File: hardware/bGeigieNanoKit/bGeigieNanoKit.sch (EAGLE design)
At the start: 5 parts

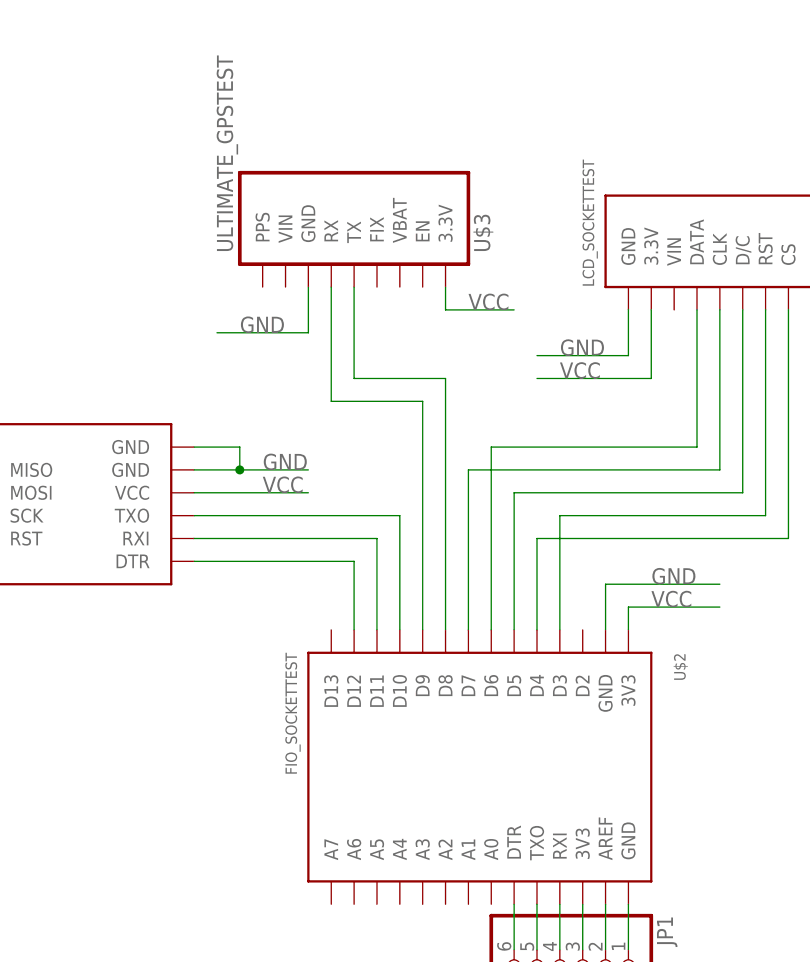
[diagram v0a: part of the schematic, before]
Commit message: library updated with full module footprints. test components removed. board updated to use new library components.
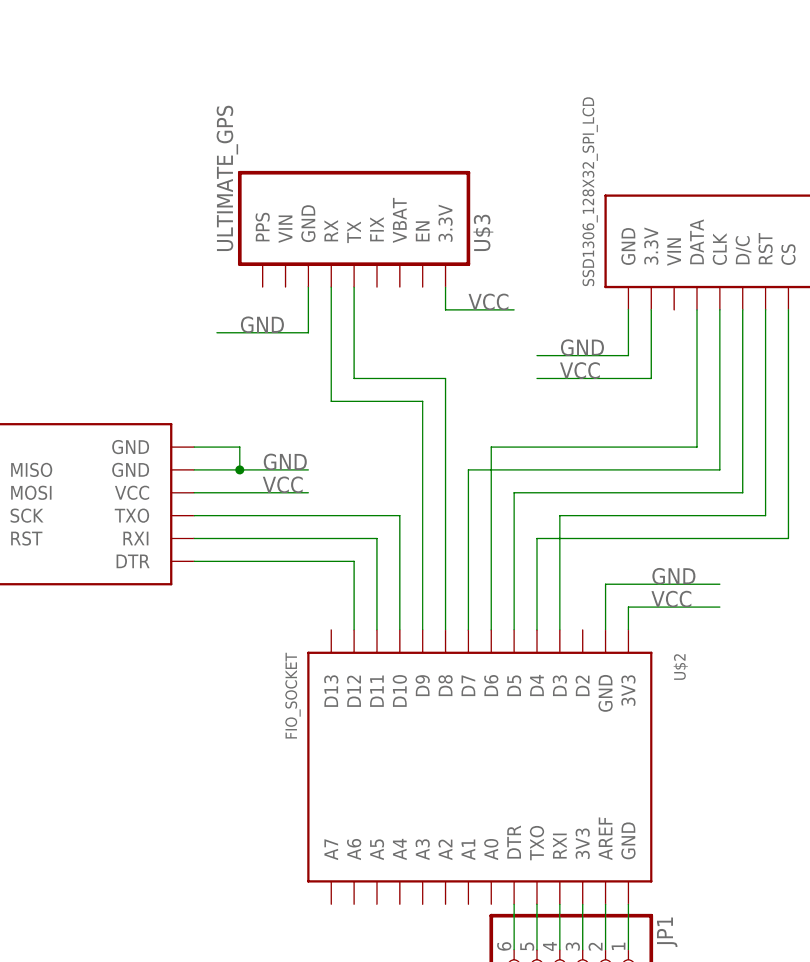
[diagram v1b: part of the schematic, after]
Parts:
- U$1: value OPENLOGTEST -> OPENLOG; device open_hw_sockets:OPENLOGTEST -> open_hw_sockets:OPENLOG
- U$2: value FIO_SOCKETTEST -> FIO_SOCKET; device open_hw_sockets:FIO_SOCKETTEST -> open_hw_sockets:FIO_SOCKET
- U$3: value ULTIMATE_GPSTEST -> ULTIMATE_GPS; device open_hw_sockets:ULTIMATE_GPSTEST -> open_hw_sockets:ULTIMATE_GPS
- U$4: value LCD_SOCKETTEST -> SSD1306_128X32_SPI_LCD; device open_hw_sockets:LCD_SOCKETTEST -> open_hw_sockets:SSD1306_128X32_SPI_LCD
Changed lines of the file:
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@@
 <parts>
 <part name="FRAME1" library="frames" deviceset="FRAME_A_L" device=""/>
-<part name="U$1" library="open_hw_sockets" deviceset="OPENLOG" device="TEST" value="OPENLOGTEST"/>
-<part name="U$4" library="open_hw_sockets" deviceset="LCD_SOCKET" device="TEST" value="LCD_SOCKETTEST"/>
-<part name="U$3" library="open_hw_sockets" deviceset="ULTIMATE_GPS" device="TEST" value="ULTIMATE_GPSTEST"/>
-<part name="U$2" library="open_hw_sockets" deviceset="FIO_SOCKET" device="TEST" value="FIO_SOCKETTEST"/>
+<part name="U$1" library="open_hw_sockets" deviceset="OPENLOG" device="" value="OPENLOG"/>
+<part name="U$4" library="open_hw_sockets" deviceset="SSD1306_128X32_SPI_LCD" device="" value="SSD1306_128X32_SPI_LCD"/>
+<part name="U$3" library="open_hw_sockets" deviceset="ULTIMATE_GPS" device="" value="ULTIMATE_GPS"/>
+<part name="U$2" library="open_hw_sockets" deviceset="FIO_SOCKET" device="" value="FIO_SOCKET"/>
 <part name="JP1" library="pinhead" deviceset="PINHD-1X6" device=""/>
 </parts>

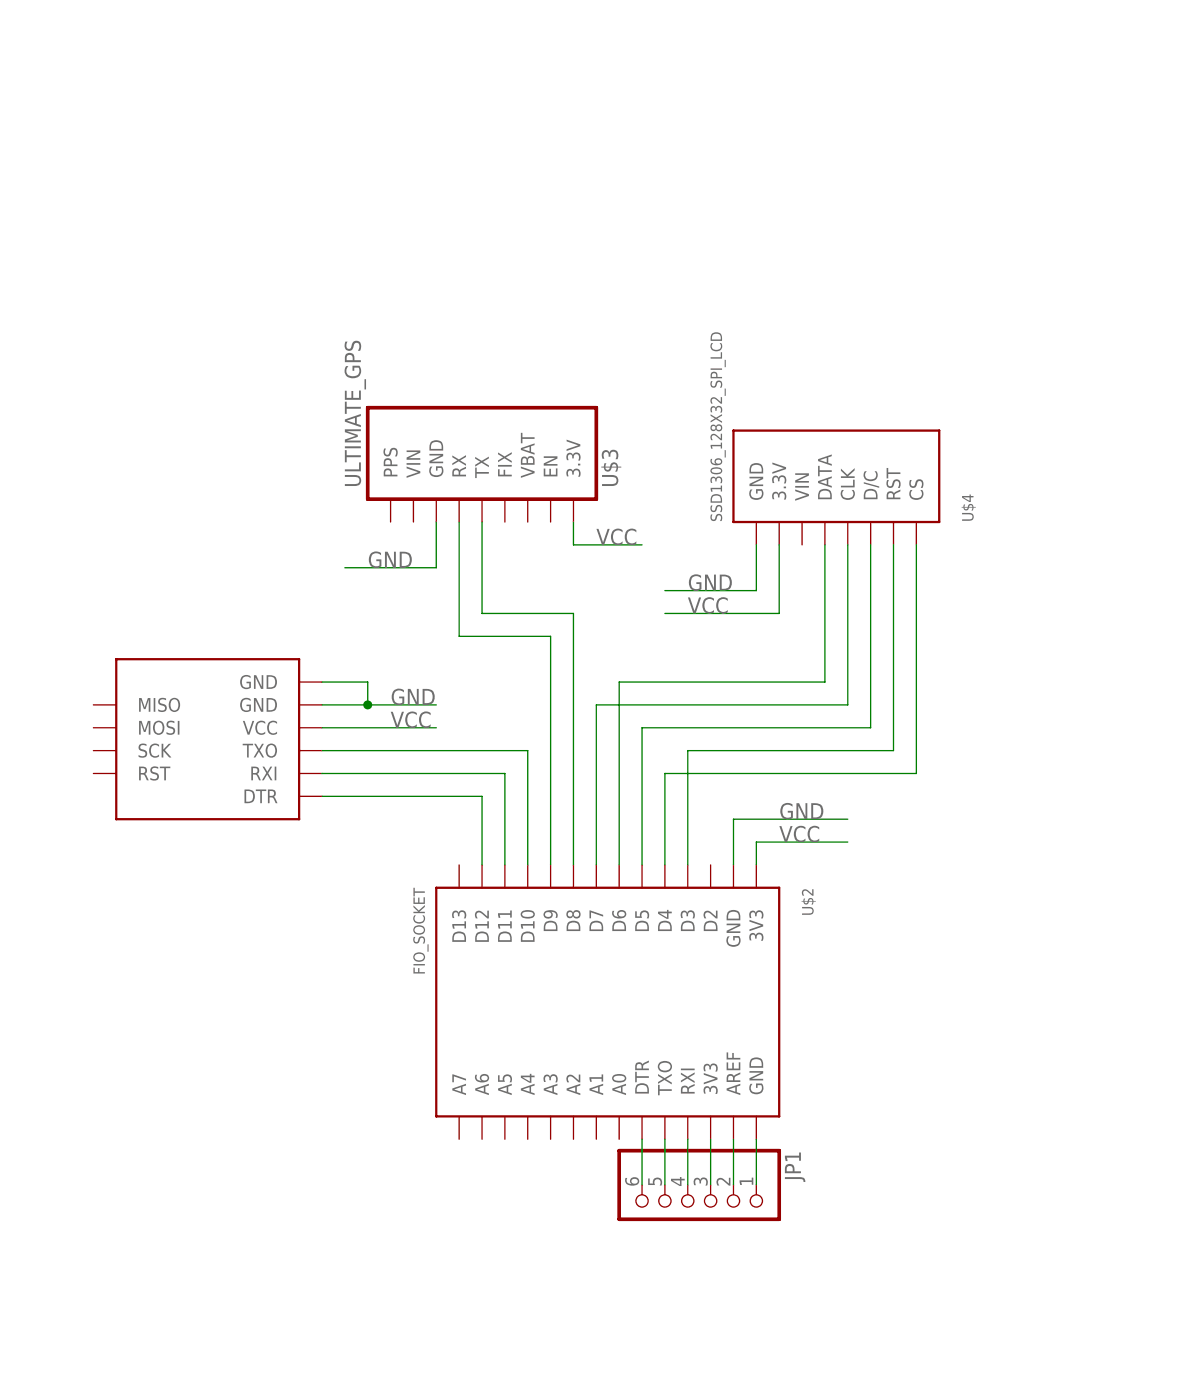
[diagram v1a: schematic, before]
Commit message: updated library footprints with single/double sided options. preliminary component placement on board to verify fit.
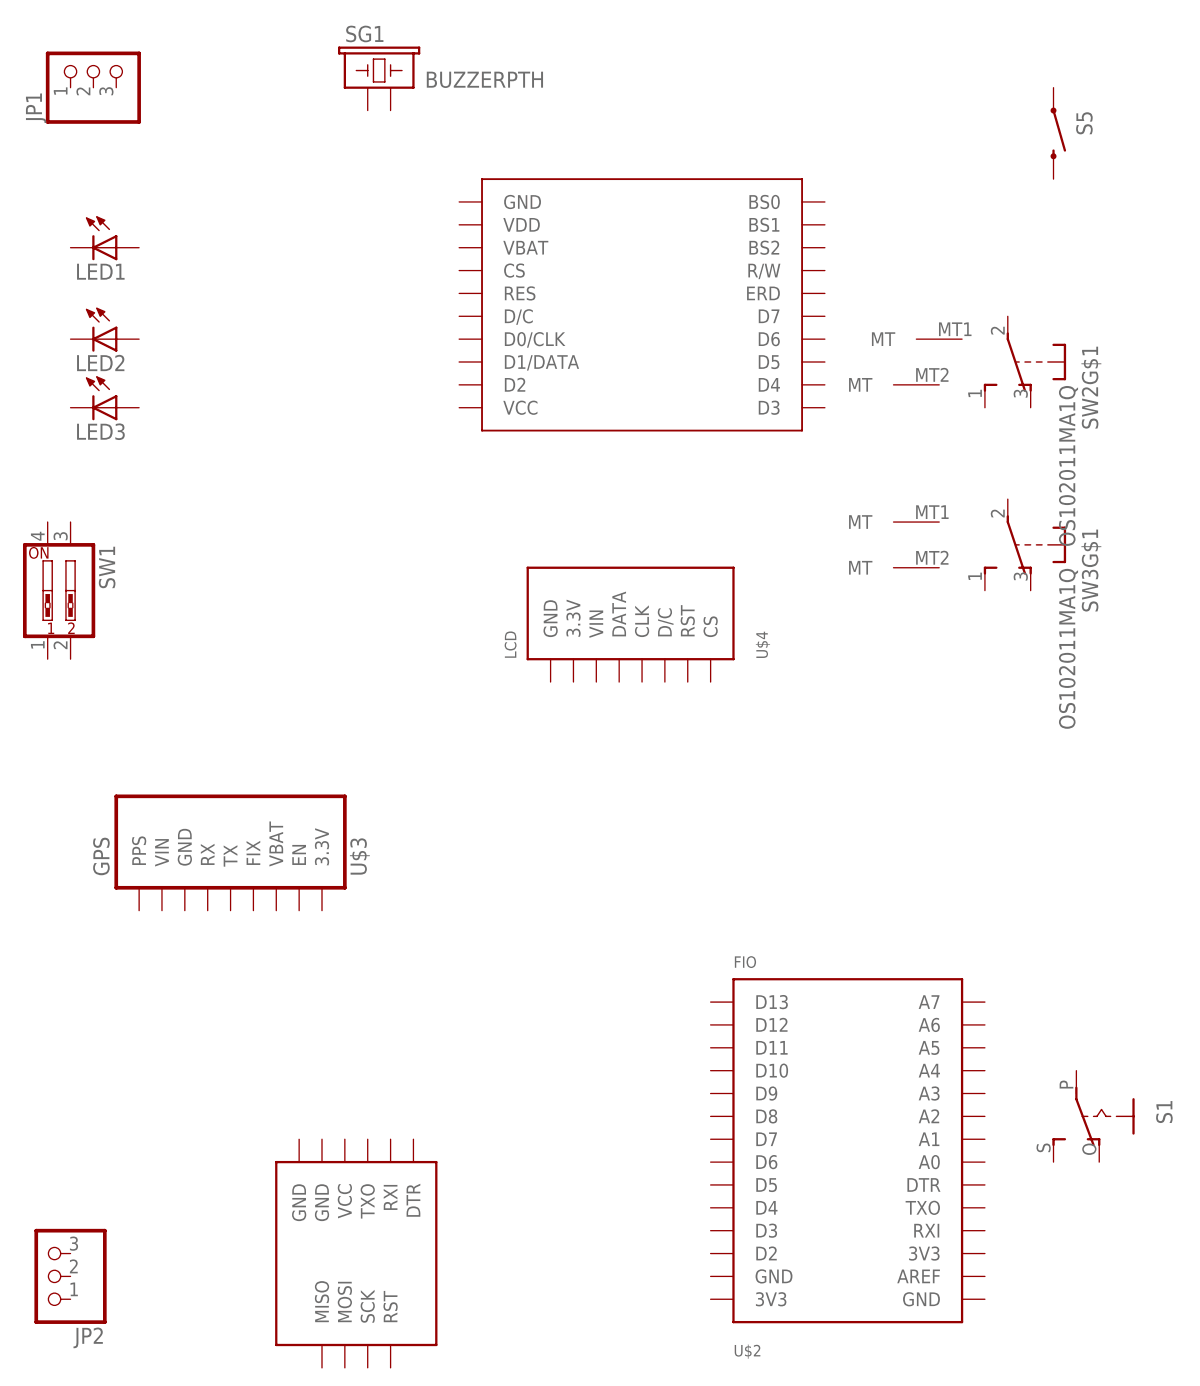
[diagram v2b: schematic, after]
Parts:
- added JP2: (no value), microbuilder:HEADER-1X376MIL
- added LED1, LED2, LED3: (no value), adafruit:LED3MM
- added S1: (no value), adafruit:EG1218S
- added S5: SWITCH-MOMENTARY-2PTH, SparkFun:SWITCH-MOMENTARY-2PTH
- added SG1: BUZZERPTH, SparkFun:BUZZERPTH
- added SW1: (no value), SparkFun:SW_DIP-2
- added SW2, SW3: OS102011MA1Q, adafruit:OS102011MA1Q
- added U$5: SSD1306_128X64_LCDTOP, open_hw_sockets:SSD1306_128X64_LCDTOP
- JP1: device pinhead:PINHD-1X6 -> microbuilder:HEADER-1X376MIL
- U$2: value FIO_SOCKET -> FIO
- U$3: value ULTIMATE_GPS -> GPS
- U$4: value SSD1306_128X32_SPI_LCD -> LCD
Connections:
- removed net GND: U$1.GND@1, U$1.GND@2, U$2.GND@1, U$3.GND, U$4.GND
- removed net N$1: U$1.DTR, U$2.D12
- removed net N$10: U$2.D4, U$4.CS
- removed net N$11: JP1.1, U$2.GND@2
- removed net N$12: JP1.2, U$2.AREF
- removed net N$13: JP1.3, U$2.3V3@2
- removed net N$14: JP1.4, U$2.RXI
- removed net N$15: JP1.5, U$2.TXO
- removed net N$16: JP1.6, U$2.DTR
- removed net N$2: U$1.RXI, U$2.D11
- removed net N$3: U$1.TXO, U$2.D10
- removed net N$4: U$2.D9, U$3.RX
- removed net N$5: U$2.D8, U$3.TX
- removed net N$6: U$2.D6, U$4.DATA
- removed net N$7: U$2.D7, U$4.CLK
- removed net N$8: U$2.D5, U$4.D/C
- removed net N$9: U$2.D3, U$4.RST
- removed net VCC: U$1.VCC, U$2.3V3@1, U$3.3.3V, U$4.3.3V
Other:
- moved on the sheet: U$2, U$3, U$4

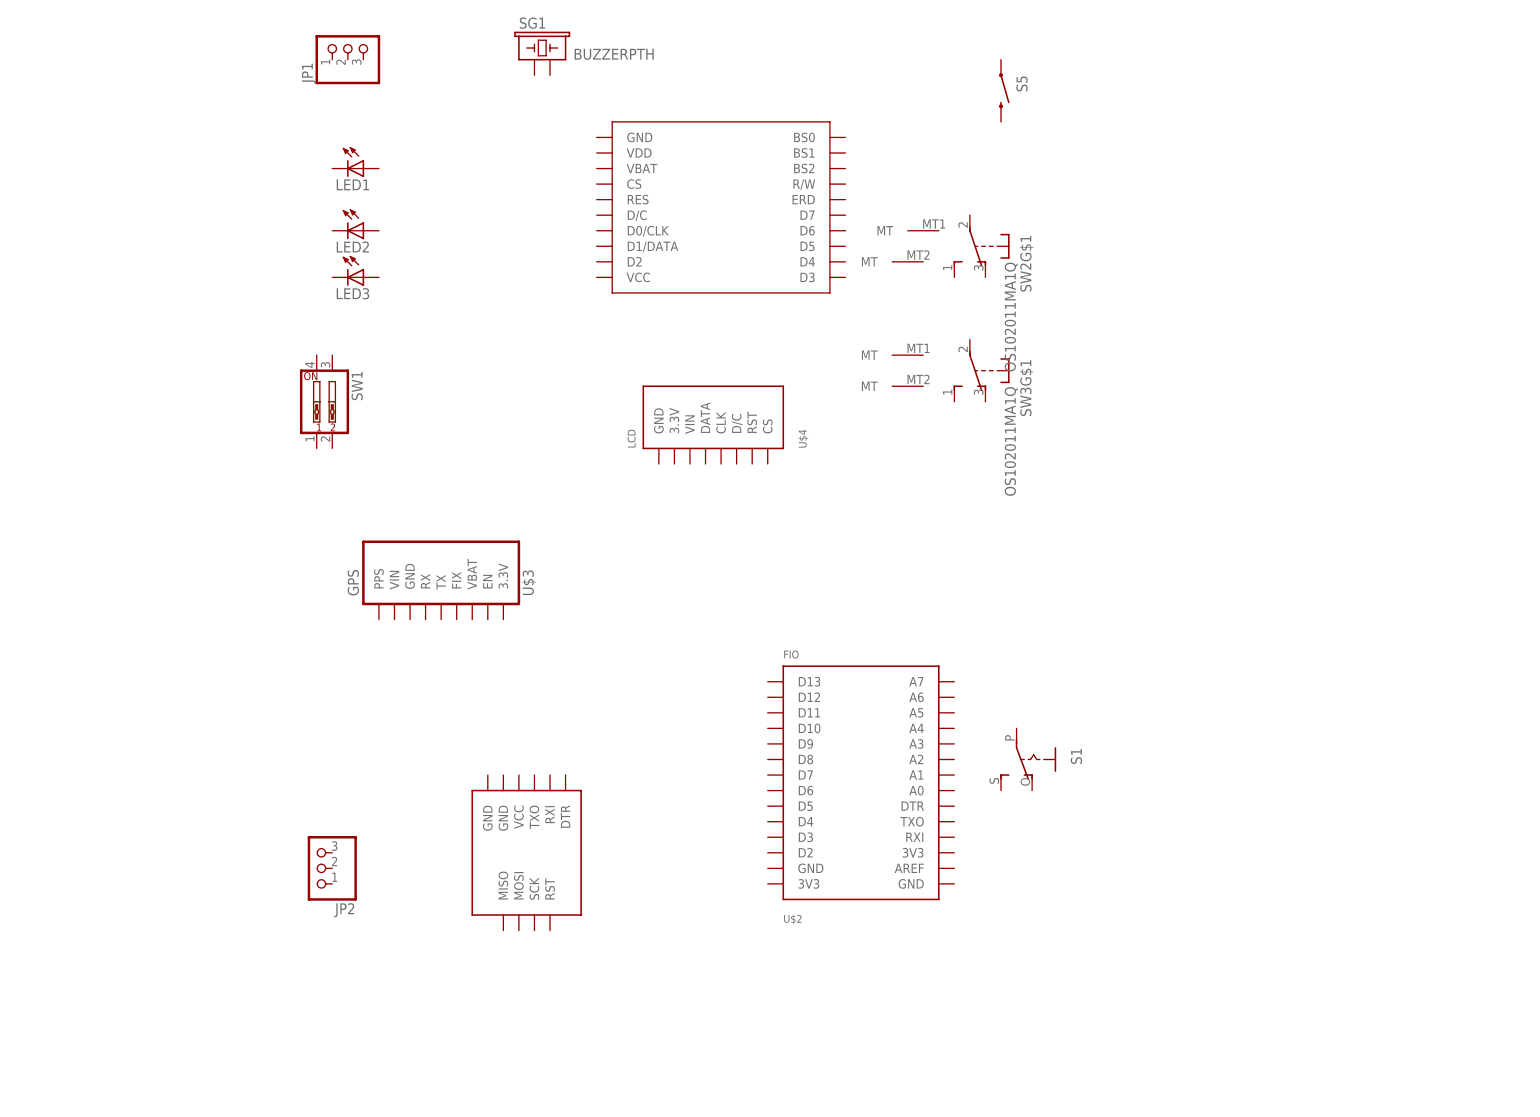
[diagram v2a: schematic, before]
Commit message: full set of components added to library. initital placement of all components.
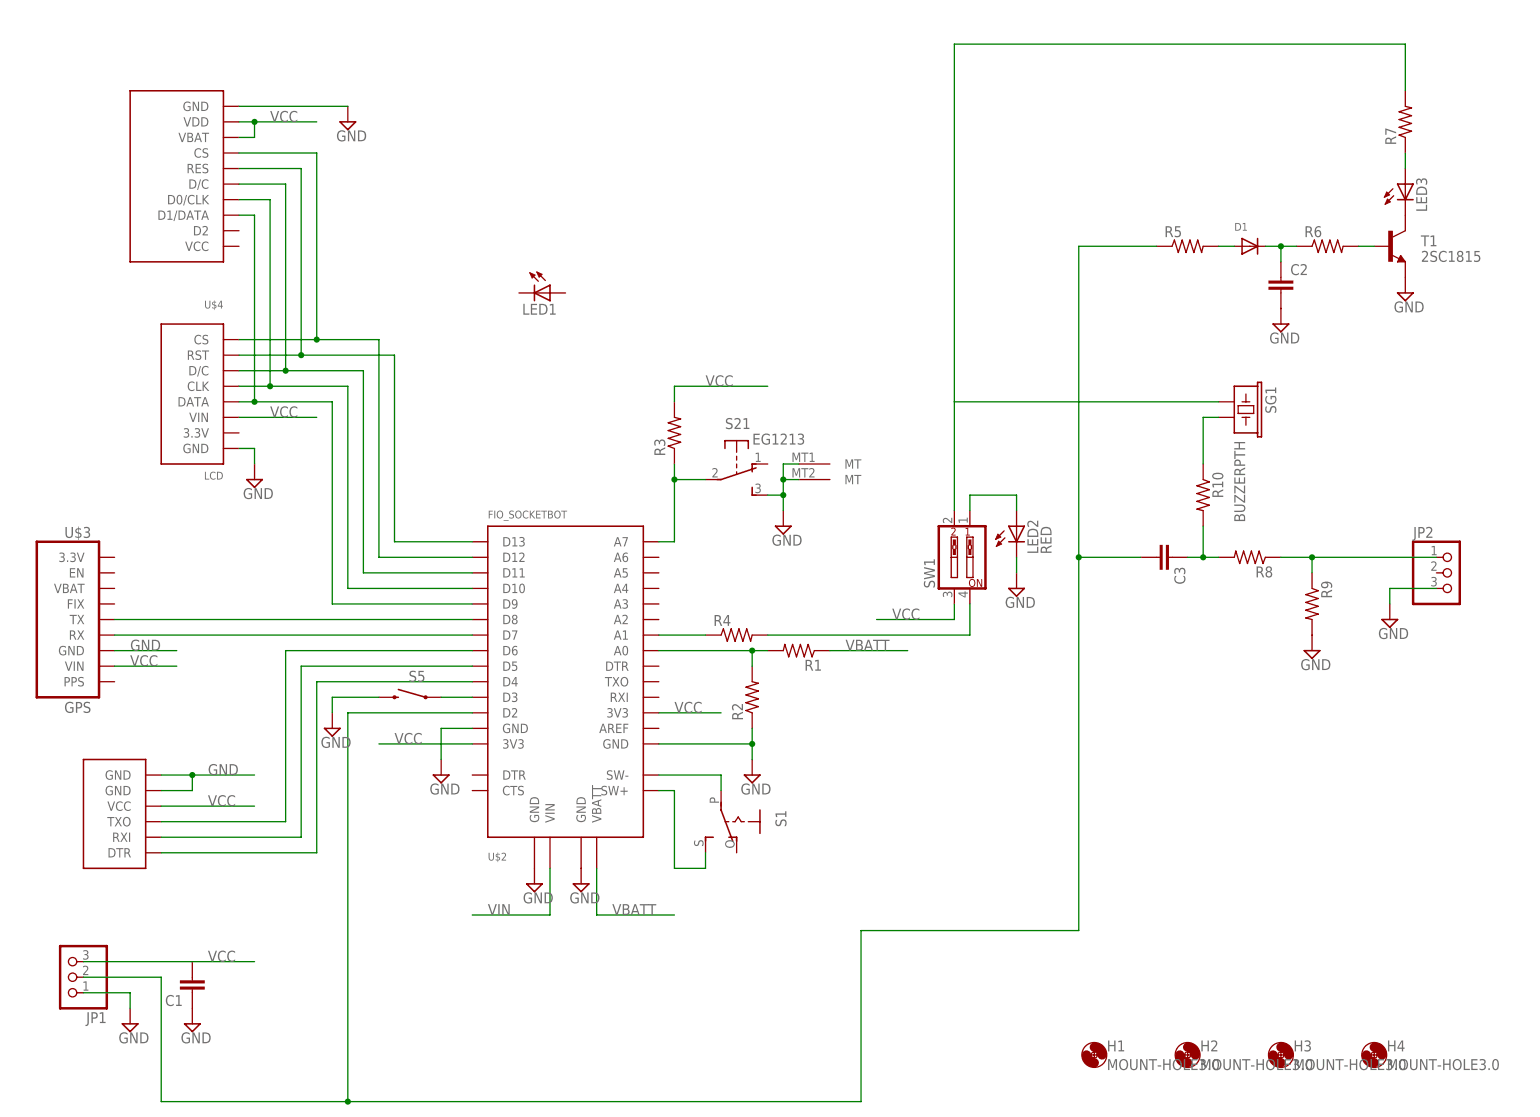
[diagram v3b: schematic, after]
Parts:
- removed SW2, SW3: OS102011MA1Q, adafruit:OS102011MA1Q
- added C1, C2, C3: (no value), rcl:C-EU050-024X044
- added D1: (no value), adafruit:DIODEDO-1N4148
- added H1, H2, H3, H4: MOUNT-HOLE3.0, holes:MOUNT-HOLE3.0
- added R1, R10, R2, R3, R4, R5, R6, R7, R8, R9: (no value), rcl:R-US_0207/10
- added S2: EG1213, adafruit:EG1213
- added T1: 2SC1815, transistor:2SC1815
- LED2: value (none) -> RED
- U$1: value OPENLOG -> OPENLOG_MIN; device open_hw_sockets:OPENLOG -> open_hw_sockets:OPENLOG_MIN
- U$2: value FIO -> FIO_SOCKETBOT; device open_hw_sockets:FIO_SOCKET -> open_hw_sockets:FIO_SOCKETBOT
- U$5: value SSD1306_128X64_LCDTOP -> SSD1306_128X64_LCD_MIN; device open_hw_sockets:SSD1306_128X64_LCDTOP -> open_hw_sockets:SSD1306_128X64_LCD_MIN
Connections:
- new net GND: C1.1, C2.2, JP1.1, JP2.3, LED2.C, R2.1, R9.2, S21.S, S2G$1.MT, S2G$2.MT, S5.2, T1.E, U$1.GND@1, U$1.GND@2, U$2.GND@1, U$2.GND@2, U$2.GND@3, U$2.GND@4, U$3.GND, U$4.GND, U$5.GND
- new net N$1: U$2.D9, U$4.DATA, U$5.D1/DATA
- new net N$10: U$1.DTR, U$2.D4
- new net N$11: R1.2, R2.2, U$2.A0
- new net N$12: S1.S, U$2.SW+
- new net N$13: S1.P, U$2.SW-
- new net N$14: R3.1, S21.P, U$2.A7
- new net N$15: R4.1, U$2.A1
- new net N$16: R4.2, SW1.4
- new net N$17: LED2.A, SW1.1
- new net N$18: C3.2, JP1.2, R5.1, U$2.D2
- new net N$19: LED3.A, R7.1
- new net N$2: U$2.D10, U$4.CLK, U$5.D0/CLK
- new net N$20: S5.1, U$2.D3
- new net N$21: R7.2, SG1.1, SW1.2
- new net N$22: LED3.C, T1.C
- new net N$23: R10.1, SG1.2
- new net N$24: C3.1, R10.2, R8.2
- new net N$25: JP2.1, R8.1, R9.1
- new net N$26: D1.A, R5.2
- new net N$27: C2.1, D1.C, R6.1
- new net N$28: R6.2, T1.B
- new net N$3: U$2.D11, U$4.D/C, U$5.D/C
- new net N$4: U$2.D12, U$4.CS, U$5.CS
- new net N$5: U$2.D13, U$4.RST, U$5.RES
- new net N$6: U$2.D8, U$3.TX
- new net N$7: U$2.D7, U$3.RX
- new net N$8: U$1.TXO, U$2.D6
- new net N$9: U$1.RXI, U$2.D5
- new net VBATT: R1.1, U$2.VBATT
- new net VCC: C1.2, JP1.3, R3.2, SW1.3, U$1.VCC, U$2.3V3@1, U$2.3V3@2, U$3.VIN, U$4.VIN, U$5.VBAT, U$5.VDD
- new net VIN: U$2.VIN
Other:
- moved on the sheet: JP1, JP2, LED1, LED2, LED3, S1, S5, SG1, SW1, U$3, U$4
